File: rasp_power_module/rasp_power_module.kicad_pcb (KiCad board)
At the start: 2 copper layers, 45.7 x 59.3 mm, 22 parts, among them J1 Conn_01x02, J2 Conn_01x05, J3 Conn_01x02, J5 Conn_01x02, J7 Conn_01x02, J8 Conn_01x02, J9 Conn_01x02, K1 G5V-1, K2 SANYOU_SRD_Form_C, Q1 S8050 J3Y

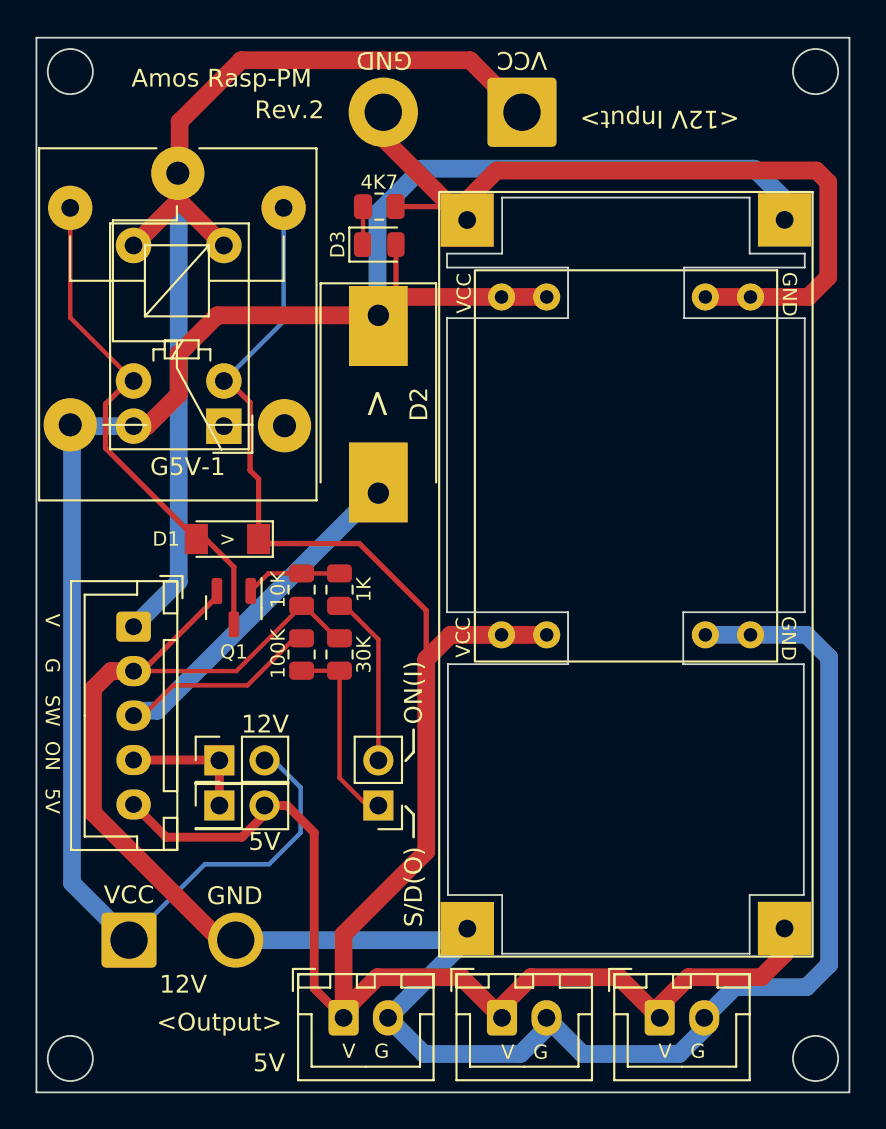
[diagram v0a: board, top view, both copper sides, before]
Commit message: rasp_pm 다이오드 변경 및 마킹 조정
Signed-off-by: Ju, Gyeong-min <jcmh74@gmail.com>
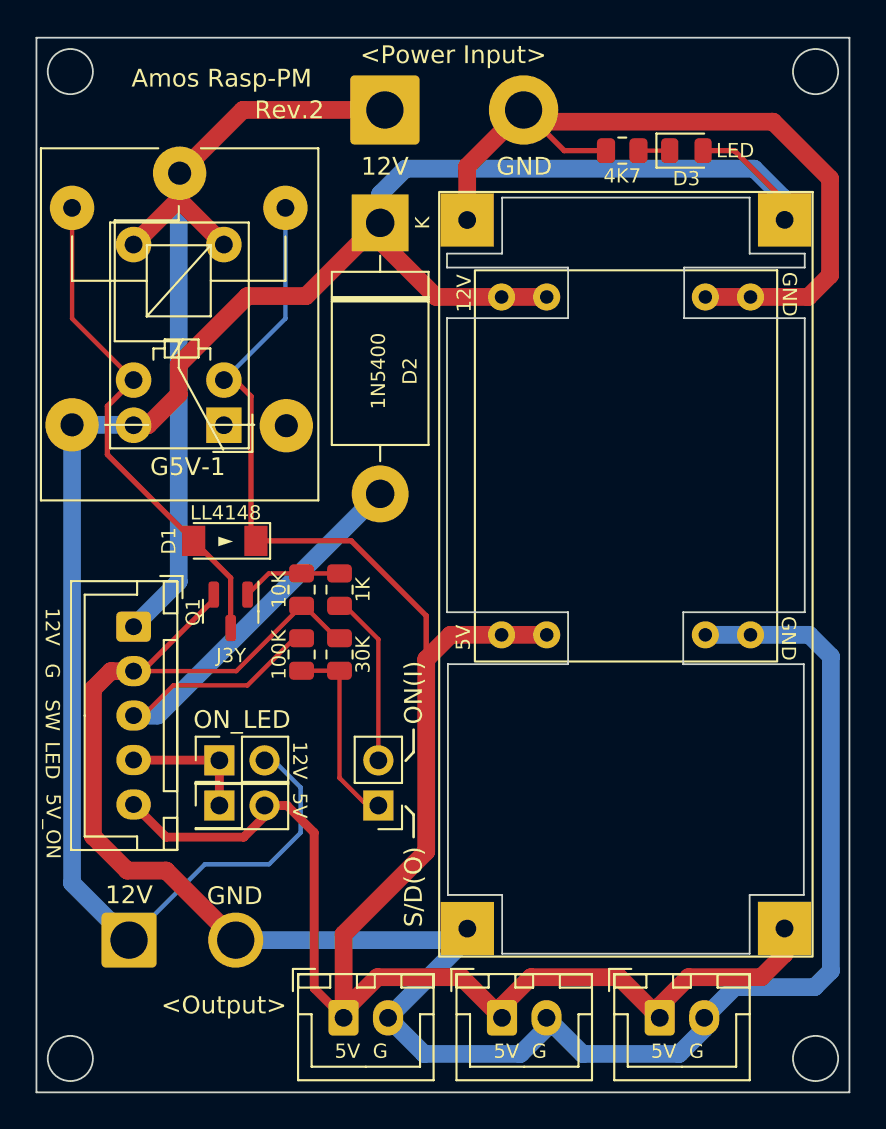
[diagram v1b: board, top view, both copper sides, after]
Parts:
- D2: value 1N4007 -> 1N5400; footprint Diode_SMD:D_SMC-RM10_Universal_Handsoldering -> Diode_THT:D_DO-201AD_P15.24mm_Horizontal
- moved D3 18.1 mm to (158.3, 63.8)
- moved R5 14.0 mm to (154.7, 63.8), turned to 0 degrees
- moved D2 10.2 mm to (141.1, 67.8)
- moved J1 7.71 mm to (141.4, 61.5), turned to 0 degrees
- moved Q1 0.27 mm to (132.7, 89.7)
- moved D1 0.18 mm to (132.4, 85.7)
- moved K2 0.10 mm to (129.8, 65.0)
- moved K1 0.05 mm to (132.3, 79.2)
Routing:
- net Relay_In: track 60.6 -> 48.7 mm
- net 12V_ON: track 113.9 -> 116.2 mm
- net InGND: track 163.6 -> 162.1 mm
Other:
- board text added: "5V G"
- board text added: "5V_ON"
- board text added: "<Power Input>"
- board text added: "G 5V"
- board text added: "J3Y"
- board text added: "LED"
- board text added: "ON_LED"
- board text added: "►"
- board text added: "◄MP1584 Out"
- board text removed: "100K"
- board text removed: "10K"
- board text removed: "1K"
- board text removed: "30K"
- board text removed: "4K7"
- board text removed: "<-MP1584 Out"
- board text removed: "<12V Input>"
- board text removed: ">"
- board text removed: "G V"
- board text removed: "ON"
- board text removed: "V"
- board text removed: "V G"
- board text removed: "VCC"

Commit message: rasp_pm 마킹 추가
Signed-off-by: Ju, Gyeong-min <jcmh74@gmail.com>
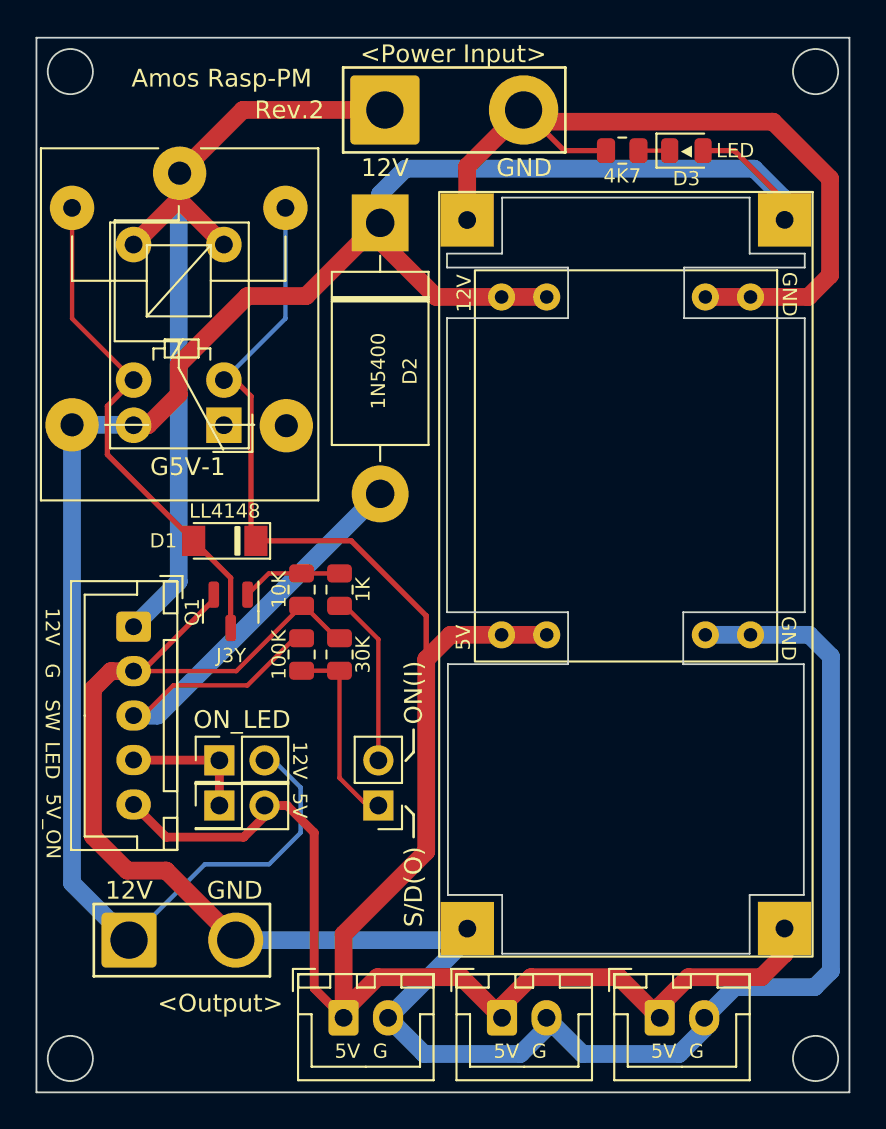
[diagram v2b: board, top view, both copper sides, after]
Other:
- board text added: "◄"
- board text removed: "►"
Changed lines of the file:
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@@
       (effects (font (size 1 1) (thickness 0.15)))
     )
-    (fp_text value "MP1584_module" (at 11.7602 2.3114 -90 unlocked) (layer "F.Fab")
-      (effects (font (size 1 1) (thickness 0.15)))
-    )
-    (fp_text user "${REFERENCE}" (at 12.0142 0.889 -90 unlocked) (layer "F.Fab")
+    (fp_text value "MP1584_module" (at 18.034 8.509 unlocked) (layer "F.Fab")
+      (effects (font (size 1 1) (thickness 0.15)))
+    )
+    (fp_text user "${REFERENCE}" (at 20.066 8.509 unlocked) (layer "F.Fab")
       (effects (font (size 1 1) (thickness 0.15)))
     )
@@
       (effects (font (size 1 1) (thickness 0.15)))
     )
-    (fp_text value "LM2596_module" (at 6.858 1.016 -90 unlocked) (layer "F.Fab")
-      (effects (font (size 1 1) (thickness 0.15)))
-    )
-    (fp_text user "${REFERENCE}" (at 6.858 -0.508 -90 unlocked) (layer "F.Fab")
+    (fp_text value "LM2596_module" (at 17.4498 0 unlocked) (layer "F.Fab")
+      (effects (font (size 1 1) (thickness 0.15)))
+    )
+    (fp_text user "${REFERENCE}" (at 19.3548 0 unlocked) (layer "F.Fab")
       (effects (font (size 1 1) (thickness 0.15)))
     )
@@
       (effects (font (size 0.8 0.8) (thickness 0.15)))
     )
-    (fp_text user "K" (at 0 -2.3876 -90) (layer "F.SilkS")
-      (effects (font (size 0.8 0.8) (thickness 0.15)))
-    )
-    (fp_text user "K" (at 0 -2.6 -90) (layer "F.Fab")
+    (fp_text user "K" (at 0.0508 -2.4384 -90) (layer "F.SilkS") hide
+      (effects (font (size 0.8 0.8) (thickness 0.15)))
+    )
+    (fp_text user "K" (at 0 -2.6 -90) (layer "F.Fab") hide
       (effects (font (size 1 1) (thickness 0.15)))
     )
@@
       (effects (font (size 1 1) (thickness 0.15)))
     )
-    (fp_text value "Conn_01x02" (at 1.778 1.1684 90) (layer "F.Fab")
+    (fp_text value "Conn_01x02" (at 1.778 1.1684 90) (layer "F.Fab") hide
       (effects (font (size 0.5 0.5) (thickness 0.125)))
     )
-    (fp_text user "${REFERENCE}" (at 0 1.27 90) (layer "F.Fab")
+    (fp_text user "${REFERENCE}" (at 0 -2.6416 180) (layer "F.Fab")
       (effects (font (size 1 1) (thickness 0.15)))
     )
@@
     (property "Sheetname" "")
     (attr smd)
-    (fp_text reference "Q1" (at 0.0508 2.1082 -90) (layer "F.SilkS")
-      (effects (font (size 0.8 0.8) (thickness 0.15)))
-    )
-    (fp_text value "S8050 J3Y" (at -0.0508 2.1082 -90) (layer "F.Fab")
+    (fp_text reference "Q1" (at 0.0508 2.159 -90) (layer "F.SilkS")
+      (effects (font (size 0.8 0.8) (thickness 0.15)))
+    )
+    (fp_text value "S8050 J3Y" (at -2.3876 0.0254) (layer "F.Fab")
       (effects (font (size 0.5 0.5) (thickness 0.125)))
     )
@@
     (property "Sheetname" "")
     (attr smd)
-    (fp_text reference "D1" (at 3.1496 0 270) (layer "F.SilkS")
-      (effects (font (size 0.8 0.8) (thickness 0.15)))
-    )
-    (fp_text value "LL4148" (at -0.0508 1.5748 180) (layer "F.SilkS")
+    (fp_text reference "D1" (at 3.4544 0) (layer "F.SilkS")
+      (effects (font (size 0.8 0.8) (thickness 0.15)))
+    )
+    (fp_text value "LL4148" (at 0 1.6764 180) (layer "F.SilkS")
       (effects (font (size 0.8 0.8) (thickness 0.15)))
     )
@@
     )
   )
+  (gr_rect (start 132.9944 84.9376) (end 133.1976 86.4616) (layer "F.SilkS") (width 0.15) (fill solid))
+  (gr_rect (start 125.0188 106.1212) (end 134.9248 110.1852) (layer "F.SilkS") (width 0.15) (fill none))
   (gr_line (start 142.554 98.0648) (end 143.002 97.5868) (layer "F.SilkS") (width 0.15))
+  (gr_rect (start 139.0396 59.0804) (end 151.5364 63.8556) (layer "F.SilkS") (width 0.15) (fill none))
   (gr_line (start 143.002 97.5868) (end 143.002 96.3168) (layer "F.SilkS") (width 0.15))
   (gr_line (start 143.002 101.092) (end 143.002 102.362) (layer "F.SilkS") (width 0.15))
@@
     (effects (font (size 1 1) (thickness 0.15)) (justify mirror))
   )
-  (gr_text "GND" (at 132.9436 105.664) (layer "B.SilkS")
+  (gr_text "GND" (at 132.9436 105.3592) (layer "B.SilkS")
     (effects (font (size 1 1) (thickness 0.15)) (justify mirror))
   )
@@
     (effects (font (size 0.8 0.8) (thickness 0.15)) (justify mirror))
   )
-  (gr_text "12V" (at 127 105.6132) (layer "B.SilkS")
+  (gr_text "12V" (at 127 105.3592) (layer "B.SilkS")
     (effects (font (size 1 1) (thickness 0.15)) (justify mirror))
   )
@@
     (effects (font (size 0.8 0.8) (thickness 0.15)))
   )
-  (gr_text "<Power Input>" (at 145.2372 58.3692) (layer "F.SilkS")
+  (gr_text "<Power Input>" (at 145.2372 58.3184) (layer "F.SilkS")
     (effects (font (size 1 1) (thickness 0.15)))
   )
-  (gr_text "GND" (at 132.9436 105.664) (layer "F.SilkS")
+  (gr_text "GND" (at 132.9436 105.3592) (layer "F.SilkS")
     (effects (font (size 1 1) (thickness 0.15)))
   )
@@
     (effects (font (size 0.8 0.8) (thickness 0.15)))
   )
-  (gr_text "12V" (at 141.388 64.643) (layer "F.SilkS")
+  (gr_text "12V" (at 141.388 64.7192) (layer "F.SilkS")
     (effects (font (size 1 1) (thickness 0.15)))
   )
@@
     (effects (font (size 0.8 0.8) (thickness 0.15)))
   )
+  (gr_text "◄" (at 158.3436 63.7032) (layer "F.SilkS")
+    (effects (font (size 1 0.6) (thickness 0.15)))
+  )
   (gr_text "GND" (at 164.1348 71.8312 270) (layer "F.SilkS")
     (effects (font (size 0.8 0.8) (thickness 0.15)))
@@
     (effects (font (size 0.8 0.8) (thickness 0.15)))
   )
-  (gr_text "►" (at 132.4356 85.6488) (layer "F.SilkS")
-    (effects (font (size 0.8 0.8) (thickness 0.15)))
-  )
   (gr_text "5V  G" (at 140.0556 114.4016) (layer "F.SilkS")
     (effects (font (size 0.8 0.8) (thickness 0.15)))
   )
-  (gr_text "12V" (at 127 105.6132) (layer "F.SilkS")
+  (gr_text "12V" (at 127 105.3592) (layer "F.SilkS")
     (effects (font (size 1 1) (thickness 0.15)))
   )
-  (gr_text "<Output>" (at 132.334 111.8108) (layer "F.SilkS")
+  (gr_text "<Output>" (at 132.1308 111.7092) (layer "F.SilkS")
     (effects (font (size 1 1) (thickness 0.15)))
   )
-  (gr_text "GND" (at 149.225 64.643) (layer "F.SilkS")
+  (gr_text "GND" (at 149.225 64.7192) (layer "F.SilkS")
     (effects (font (size 1 1) (thickness 0.15)))
   )
